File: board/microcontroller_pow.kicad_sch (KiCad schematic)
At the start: 15 parts

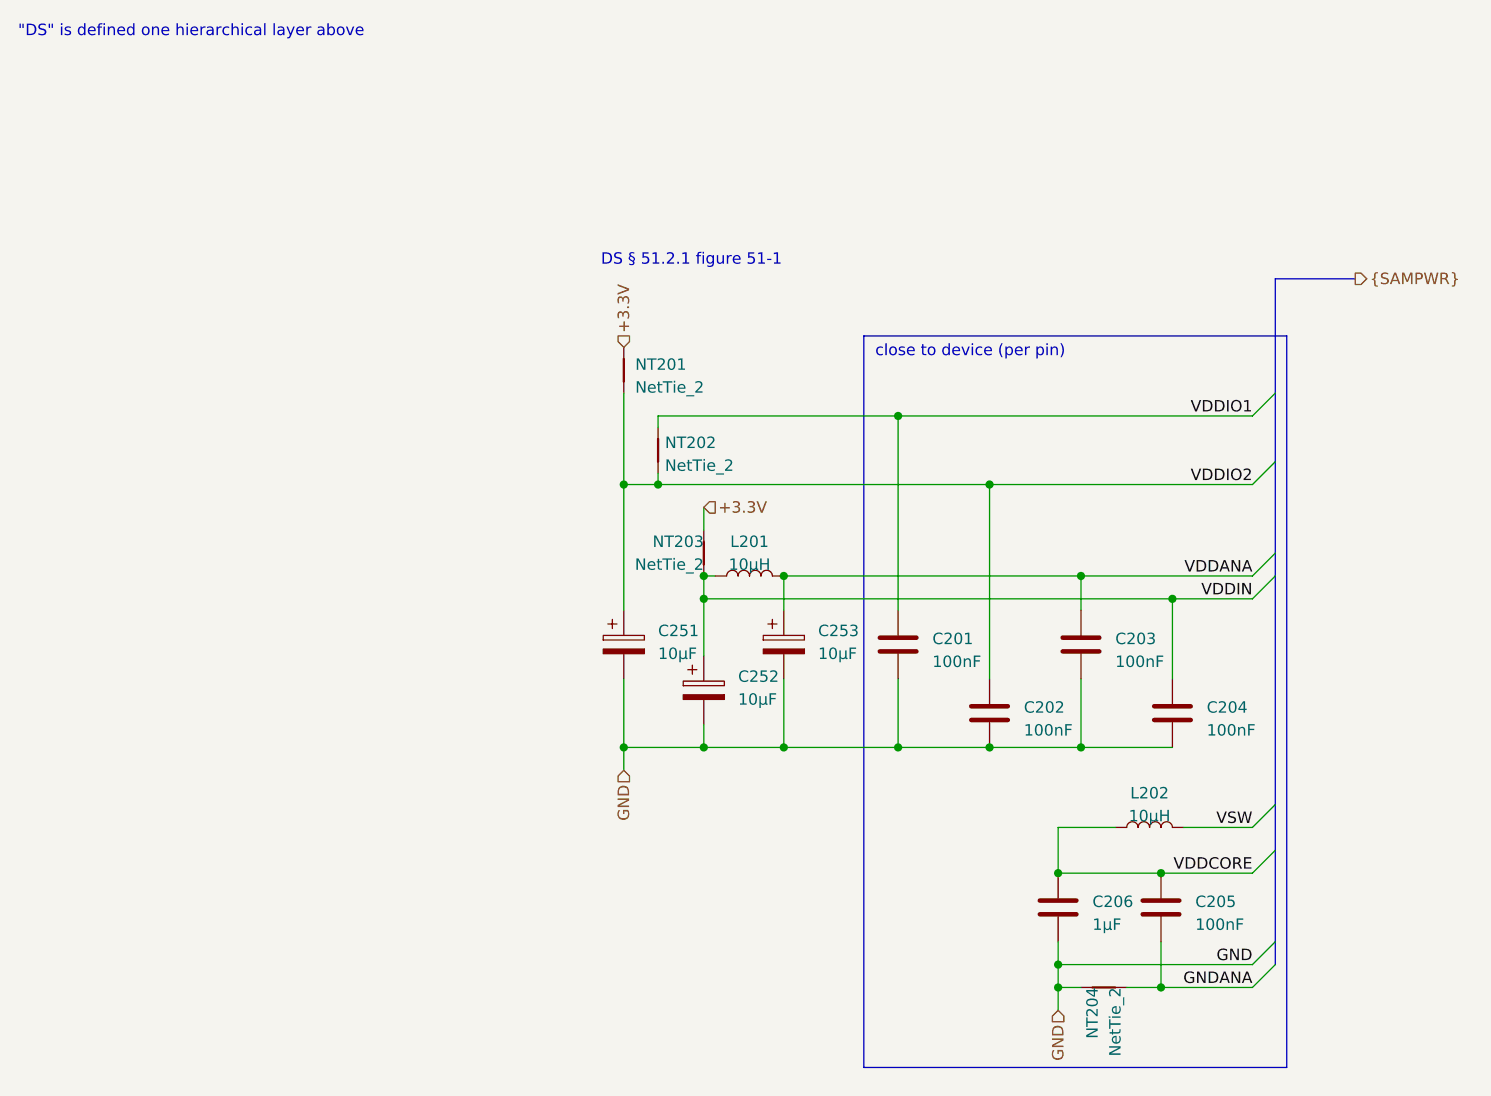
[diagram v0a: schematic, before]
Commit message: redo board with STM32G0B0CET
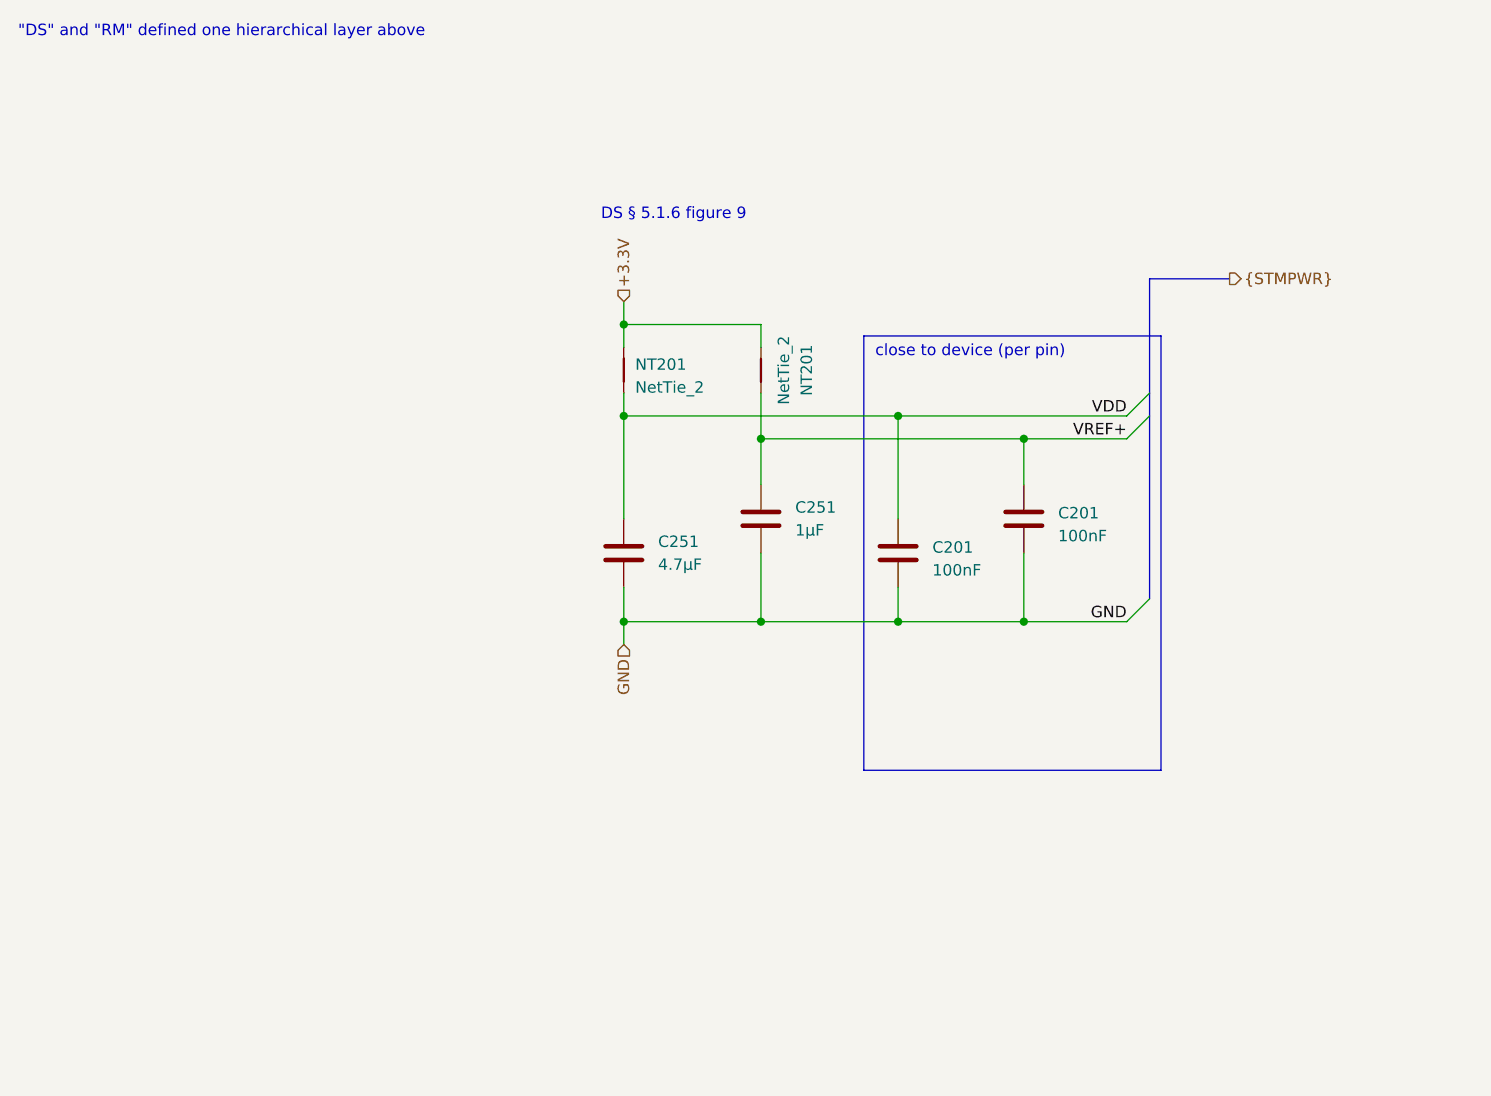
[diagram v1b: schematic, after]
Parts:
- removed C202, C203, C204, C205: 100nF, Capacitor_SMD:C_0402_1005Metric, symbol Device:C
- removed C206: 1µF, Capacitor_SMD:C_0603_1608Metric, symbol Device:C
- removed C252, C253: 10µF, Capacitor_SMD:C_0603_1608Metric, symbol Device:C_Polarized
- removed L201, L202: 10µH, Inductor_SMD:L_1206_3216Metric, symbol Device:L
- removed NT202, NT203, NT204: NetTie_2, NetTie:NetTie-2_SMD_Pad0.5mm, symbol Device:NetTie_2
- added C201: 100nF, Capacitor_SMD:C_0402_1005Metric, symbol Device:C
- added C251: 1µF, Capacitor_SMD:C_0603_1608Metric, symbol Device:C
- added NT201: NetTie_2, NetTie:NetTie-2_SMD_Pad0.5mm, symbol Device:NetTie_2
- C251: value 10µF -> 4.7µF; symbol Device:C_Polarized -> Device:C; LCSC C19702 -> C19666
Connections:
- net VDDIO2 is gone; now on net VDD: C251.1, NT201.1
- net +3.3V: now also NT201.1
- net GND: now also C201.2, C251.2
- net VDDIO1 renamed VDD
- new net VREF+: C201.1, C251.1, NT201.2
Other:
- note added: ""DS" and "RM" defined one hierarchical layer above"
- note added: "DS § 5.1.6 figure 9"
- note removed: ""DS" is defined one hierarchical layer above"
- note removed: "DS § 51.2.1 figure 51-1"
- moved on the sheet: C201
